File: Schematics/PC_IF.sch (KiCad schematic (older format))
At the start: 4 parts

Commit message: annotate
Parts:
- gave numbers to parts that had none: 4
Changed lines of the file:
@@
 AR Path="/5D2C0CA7/5DD0E967" Ref="U?"  Part="1"
 AR Path="/5D7BE200/5DD0E967" Ref="U?"  Part="1"
-AR Path="/5D8005AF/5D833E4B/5DD0E967" Ref="U?"  Part="1"
-F 0 "U?" H 5250 3350 50  0000 C CNN
+AR Path="/5D8005AF/5D833E4B/5DD0E967" Ref="U24"  Part="1"
+F 0 "U24" H 5250 3350 50  0000 C CNN
 F 1 "74F377" H 5250 3250 50  0000 C CNN
 F 2 "" H 5500 2550 50  0001 C CNN
@@
 AR Path="/5D2C0CA7/5DD0E9D6" Ref="U?"  Part="1"
 AR Path="/5D7BE200/5DD0E9D6" Ref="U?"  Part="1"
-AR Path="/5D8005AF/5D833E4B/5DD0E9D6" Ref="U?"  Part="1"
-F 0 "U?" H 5250 5500 50  0000 C CNN
+AR Path="/5D8005AF/5D833E4B/5DD0E9D6" Ref="U25"  Part="1"
+F 0 "U25" H 5250 5500 50  0000 C CNN
 F 1 "74F377" H 5250 5400 50  0000 C CNN
 F 2 "" H 5500 4700 50  0001 C CNN
@@
 $EndComp
 $Comp
-L power:VCC #PWR?
+L power:VCC #PWR0150
 U 1 1 5DD10B91
 P 5500 1750
-F 0 "#PWR?" H 5500 1600 50  0001 C CNN
+F 0 "#PWR0150" H 5500 1600 50  0001 C CNN
 F 1 "VCC" H 5517 1923 50  0000 C CNN
 F 2 "" H 5500 1750 50  0001 C CNN
@@
 $EndComp
 $Comp
-L power:VCC #PWR?
+L power:VCC #PWR0151
 U 1 1 5DD11404
 P 5500 3900
-F 0 "#PWR?" H 5500 3750 50  0001 C CNN
+F 0 "#PWR0151" H 5500 3750 50  0001 C CNN
 F 1 "VCC" H 5517 4073 50  0000 C CNN
 F 2 "" H 5500 3900 50  0001 C CNN
@@
 $EndComp
 $Comp
-L power:GND #PWR?
+L power:GND #PWR0152
 U 1 1 5DD11B50
 P 5500 3350
-F 0 "#PWR?" H 5500 3100 50  0001 C CNN
+F 0 "#PWR0152" H 5500 3100 50  0001 C CNN
 F 1 "GND" H 5505 3177 50  0000 C CNN
 F 2 "" H 5500 3350 50  0001 C CNN
@@
 $EndComp
 $Comp
-L power:GND #PWR?
+L power:GND #PWR0153
 U 1 1 5DD12126
 P 5500 5500
-F 0 "#PWR?" H 5500 5250 50  0001 C CNN
+F 0 "#PWR0153" H 5500 5250 50  0001 C CNN
 F 1 "GND" H 5505 5327 50  0000 C CNN
 F 2 "" H 5500 5500 50  0001 C CNN
@@
 	5000 5100 3400 5100
 $Comp
-L power:GND #PWR?
+L power:GND #PWR0154
 U 1 1 5DD12CA4
 P 5000 5200
-F 0 "#PWR?" H 5000 4950 50  0001 C CNN
+F 0 "#PWR0154" H 5000 4950 50  0001 C CNN
 F 1 "GND" V 5005 5072 50  0000 R CNN
 F 2 "" H 5000 5200 50  0001 C CNN
@@
 $EndComp
 $Comp
-L power:GND #PWR?
+L power:GND #PWR0155
 U 1 1 5DD131DF
 P 5000 3050
-F 0 "#PWR?" H 5000 2800 50  0001 C CNN
+F 0 "#PWR0155" H 5000 2800 50  0001 C CNN
 F 1 "GND" V 5005 2922 50  0000 R CNN
 F 2 "" H 5000 3050 50  0001 C CNN
@@
 	8850 5500 6600 5500
 $Comp
-L Device:C C?
+L Device:C C21
 U 1 1 5DD31495
 P 1000 7150
-F 0 "C?" H 1115 7196 50  0000 L CNN
+F 0 "C21" H 1115 7196 50  0000 L CNN
 F 1 "100nF" H 1115 7105 50  0000 L CNN
 F 2 "" H 1038 7000 50  0001 C CNN
@@
 $EndComp
 $Comp
-L Device:C C?
+L Device:C C22
 U 1 1 5DD3149B
 P 1500 7150
-F 0 "C?" H 1615 7196 50  0000 L CNN
+F 0 "C22" H 1615 7196 50  0000 L CNN
 F 1 "100nF" H 1615 7105 50  0000 L CNN
 F 2 "" H 1538 7000 50  0001 C CNN
@@
 $EndComp
 $Comp
-L power:GND #PWR?
+L power:GND #PWR0156
 U 1 1 5DD314A1
 P 1000 7300
-F 0 "#PWR?" H 1000 7050 50  0001 C CNN
+F 0 "#PWR0156" H 1000 7050 50  0001 C CNN
 F 1 "GND" H 1005 7127 50  0000 C CNN
 F 2 "" H 1000 7300 50  0001 C CNN
@@
 $EndComp
 $Comp
-L power:VCC #PWR?
+L power:VCC #PWR0157
 U 1 1 5DD314A7
 P 1000 7000
-F 0 "#PWR?" H 1000 6850 50  0001 C CNN
+F 0 "#PWR0157" H 1000 6850 50  0001 C CNN
 F 1 "VCC" H 1017 7173 50  0000 C CNN
 F 2 "" H 1000 7000 50  0001 C CNN

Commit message: Add footprints to all decoupling caps
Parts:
- C21, C22: footprint (none) -> Capacitor_THT:C_Disc_D4.3mm_W1.9mm_P5.00mm
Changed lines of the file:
@@
 F 0 "C21" H 1115 7196 50  0000 L CNN
 F 1 "100nF" H 1115 7105 50  0000 L CNN
-F 2 "" H 1038 7000 50  0001 C CNN
+F 2 "Capacitor_THT:C_Disc_D4.3mm_W1.9mm_P5.00mm" H 1038 7000 50  0001 C CNN
 F 3 "~" H 1000 7150 50  0001 C CNN
 	1    1000 7150
@@
 F 0 "C22" H 1615 7196 50  0000 L CNN
 F 1 "100nF" H 1615 7105 50  0000 L CNN
-F 2 "" H 1538 7000 50  0001 C CNN
+F 2 "Capacitor_THT:C_Disc_D4.3mm_W1.9mm_P5.00mm" H 1538 7000 50  0001 C CNN
 F 3 "~" H 1500 7150 50  0001 C CNN
 	1    1500 7150

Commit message: Assign a bunch more footprints. All are assigned now.
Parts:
- U24, U25: footprint (none) -> Package_DIP:DIP-20_W7.62mm
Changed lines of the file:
@@
 F 0 "U24" H 5250 3350 50  0000 C CNN
 F 1 "74F377" H 5250 3250 50  0000 C CNN
-F 2 "" H 5500 2550 50  0001 C CNN
+F 2 "Package_DIP:DIP-20_W7.62mm" H 5500 2550 50  0001 C CNN
 F 3 "http://www.ti.com/lit/gpn/sn74LS377" H 5500 2550 50  0001 C CNN
 	1    5500 2550
@@
 F 0 "U25" H 5250 5500 50  0000 C CNN
 F 1 "74F377" H 5250 5400 50  0000 C CNN
-F 2 "" H 5500 4700 50  0001 C CNN
+F 2 "Package_DIP:DIP-20_W7.62mm" H 5500 4700 50  0001 C CNN
 F 3 "http://www.ti.com/lit/gpn/sn74LS377" H 5500 4700 50  0001 C CNN
 	1    5500 4700

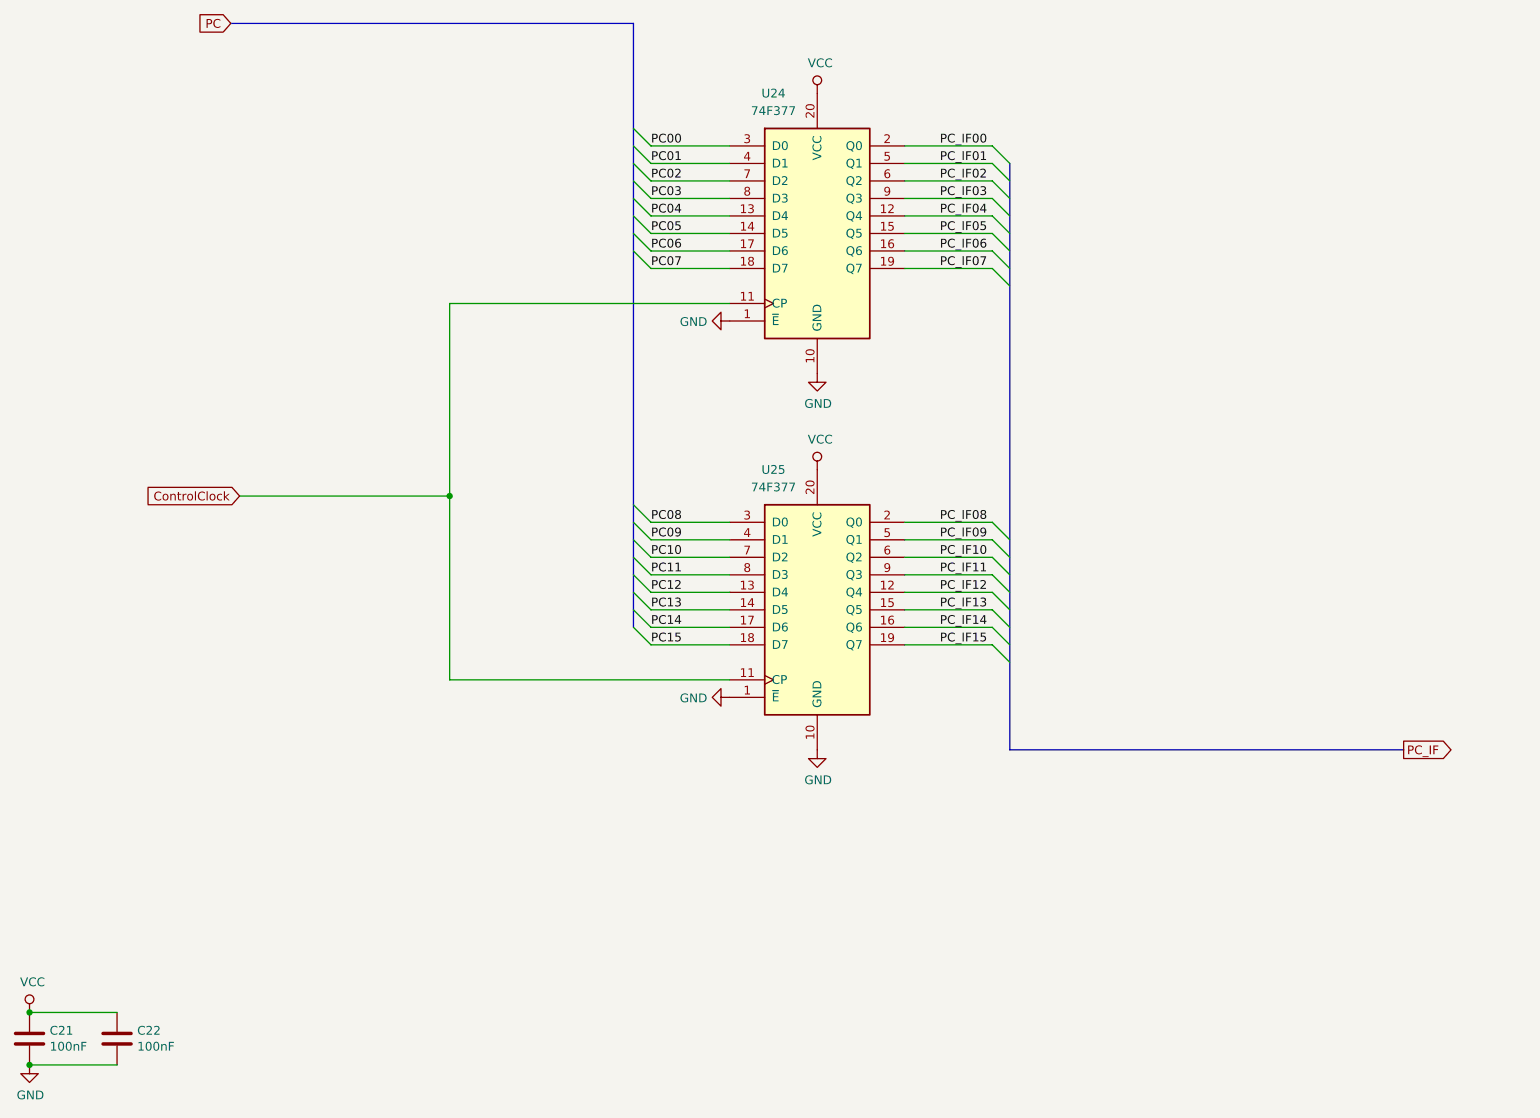
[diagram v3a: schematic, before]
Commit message: My buses were not named according the rules in the Eeschema manual.
Buses which connect to global labels must be named specially.
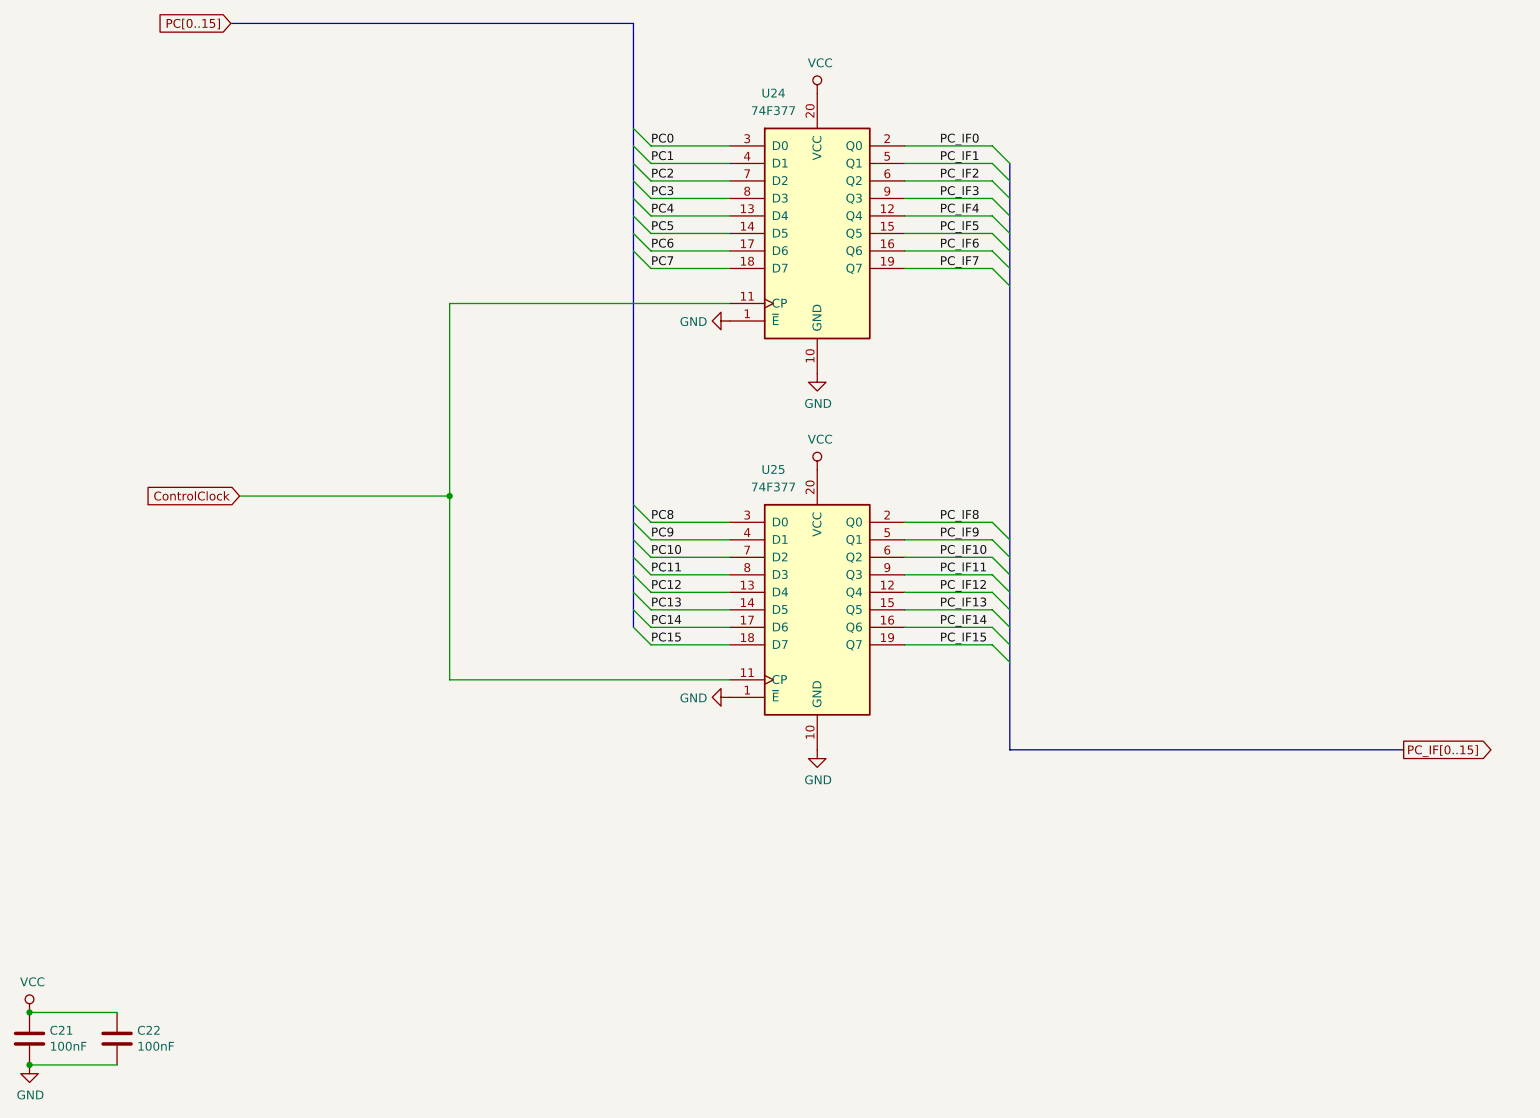
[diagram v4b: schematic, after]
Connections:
- net PC00 renamed PC0
- net PC01 renamed PC1
- net PC02 renamed PC2
- net PC03 renamed PC3
- net PC04 renamed PC4
- net PC05 renamed PC5
- net PC06 renamed PC6
- net PC07 renamed PC7
- net PC08 renamed PC8
- net PC09 renamed PC9
- net PC_IF00 renamed PC_IF0
- net PC_IF01 renamed PC_IF1
- net PC_IF02 renamed PC_IF2
- net PC_IF03 renamed PC_IF3
- net PC_IF04 renamed PC_IF4
- net PC_IF05 renamed PC_IF5
- net PC_IF06 renamed PC_IF6
- net PC_IF07 renamed PC_IF7
- net PC_IF08 renamed PC_IF8
- net PC_IF09 renamed PC_IF9
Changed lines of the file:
@@
 	3400 4050 3400 5100
 Text GLabel 2150 1350 0    50   Input ~ 0
-PC
+PC[0..15]
 Entry Wire Line
 	4550 2050 4450 1950
@@
 	4550 2050 5000 2050
 Text Label 4550 2050 0    50   ~ 0
-PC00
+PC0
 Text Label 4550 2150 0    50   ~ 0
-PC01
+PC1
 Text Label 4550 2250 0    50   ~ 0
-PC02
+PC2
 Text Label 4550 2350 0    50   ~ 0
-PC03
+PC3
 Text Label 4550 2450 0    50   ~ 0
-PC04
+PC4
 Text Label 4550 2550 0    50   ~ 0
-PC05
+PC5
 Text Label 4550 2650 0    50   ~ 0
-PC06
+PC6
 Text Label 4550 2750 0    50   ~ 0
-PC07
+PC7
 Text Label 4550 4200 0    50   ~ 0
-PC08
+PC8
 Text Label 4550 4300 0    50   ~ 0
-PC09
+PC9
 Text Label 4550 4400 0    50   ~ 0
 PC10
@@
 	6500 4900 6000 4900
 Text Label 6200 2050 0    50   ~ 0
-PC_IF00
+PC_IF0
 Text Label 6200 2150 0    50   ~ 0
-PC_IF01
+PC_IF1
 Text Label 6200 2250 0    50   ~ 0
-PC_IF02
+PC_IF2
 Text Label 6200 2350 0    50   ~ 0
-PC_IF03
+PC_IF3
 Text Label 6200 2450 0    50   ~ 0
-PC_IF04
+PC_IF4
 Text Label 6200 2550 0    50   ~ 0
-PC_IF05
+PC_IF5
 Text Label 6200 2650 0    50   ~ 0
-PC_IF06
+PC_IF6
 Text Label 6200 2750 0    50   ~ 0
-PC_IF07
+PC_IF7
 Text Label 6200 4200 0    50   ~ 0
-PC_IF08
+PC_IF8
 Text Label 6200 4300 0    50   ~ 0
-PC_IF09
+PC_IF9
 Text Label 6200 4400 0    50   ~ 0
 PC_IF10
@@
 PC_IF15
 Text GLabel 8850 5500 2    50   Output ~ 0
-PC_IF
+PC_IF[0..15]
 Wire Bus Line
 	8850 5500 6600 5500

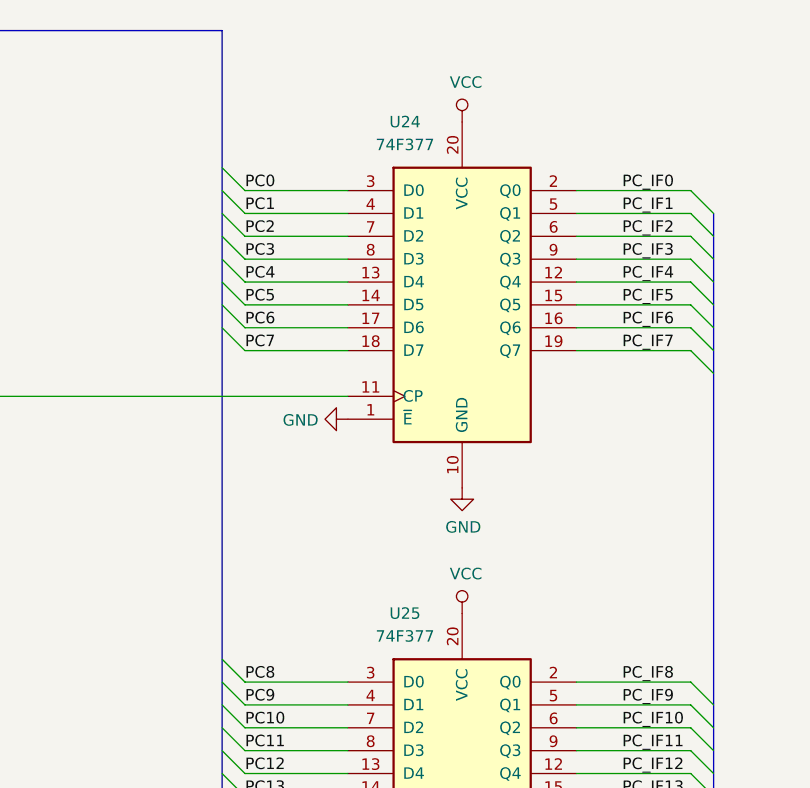
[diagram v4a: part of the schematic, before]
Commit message: Add unused IC units to Output Display to ensure no ICs are shared with other modules.
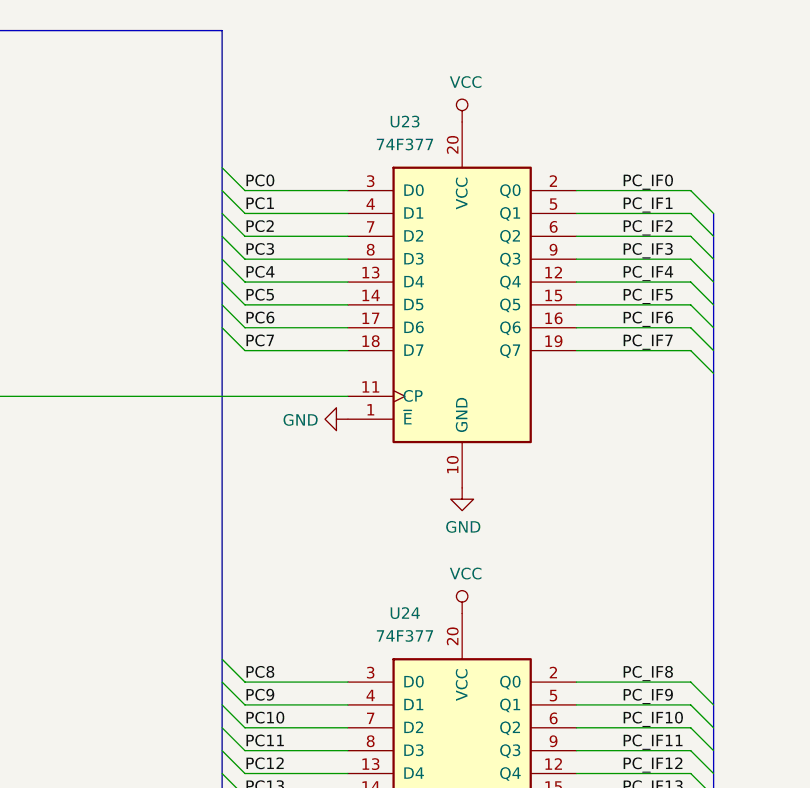
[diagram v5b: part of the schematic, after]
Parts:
- renumbered U24 to U23, U25 to U24
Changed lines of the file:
@@
 AR Path="/5D2C0CA7/5DD0E967" Ref="U?"  Part="1"
 AR Path="/5D7BE200/5DD0E967" Ref="U?"  Part="1"
-AR Path="/5D8005AF/5D833E4B/5DD0E967" Ref="U24"  Part="1"
-F 0 "U24" H 5250 3350 50  0000 C CNN
+AR Path="/5D8005AF/5D833E4B/5DD0E967" Ref="U23"  Part="1"
+F 0 "U23" H 5250 3350 50  0000 C CNN
 F 1 "74F377" H 5250 3250 50  0000 C CNN
 F 2 "Package_DIP:DIP-20_W7.62mm" H 5500 2550 50  0001 C CNN
@@
 AR Path="/5D2C0CA7/5DD0E9D6" Ref="U?"  Part="1"
 AR Path="/5D7BE200/5DD0E9D6" Ref="U?"  Part="1"
-AR Path="/5D8005AF/5D833E4B/5DD0E9D6" Ref="U25"  Part="1"
-F 0 "U25" H 5250 5500 50  0000 C CNN
+AR Path="/5D8005AF/5D833E4B/5DD0E9D6" Ref="U24"  Part="1"
+F 0 "U24" H 5250 5500 50  0000 C CNN
 F 1 "74F377" H 5250 5400 50  0000 C CNN
 F 2 "Package_DIP:DIP-20_W7.62mm" H 5500 4700 50  0001 C CNN
@@
 $EndComp
 $Comp
-L power:VCC #PWR0150
+L power:VCC #PWR054
 U 1 1 5DD10B91
 P 5500 1750
-F 0 "#PWR0150" H 5500 1600 50  0001 C CNN
+F 0 "#PWR054" H 5500 1600 50  0001 C CNN
 F 1 "VCC" H 5517 1923 50  0000 C CNN
 F 2 "" H 5500 1750 50  0001 C CNN
@@
 $EndComp
 $Comp
-L power:VCC #PWR0151
+L power:VCC #PWR056
 U 1 1 5DD11404
 P 5500 3900
-F 0 "#PWR0151" H 5500 3750 50  0001 C CNN
+F 0 "#PWR056" H 5500 3750 50  0001 C CNN
 F 1 "VCC" H 5517 4073 50  0000 C CNN
 F 2 "" H 5500 3900 50  0001 C CNN
@@
 $EndComp
 $Comp
-L power:GND #PWR0152
+L power:GND #PWR055
 U 1 1 5DD11B50
 P 5500 3350
-F 0 "#PWR0152" H 5500 3100 50  0001 C CNN
+F 0 "#PWR055" H 5500 3100 50  0001 C CNN
 F 1 "GND" H 5505 3177 50  0000 C CNN
 F 2 "" H 5500 3350 50  0001 C CNN
@@
 $EndComp
 $Comp
-L power:GND #PWR0153
+L power:GND #PWR057
 U 1 1 5DD12126
 P 5500 5500
-F 0 "#PWR0153" H 5500 5250 50  0001 C CNN
+F 0 "#PWR057" H 5500 5250 50  0001 C CNN
 F 1 "GND" H 5505 5327 50  0000 C CNN
 F 2 "" H 5500 5500 50  0001 C CNN
@@
 	5000 5100 3400 5100
 $Comp
-L power:GND #PWR0154
+L power:GND #PWR053
 U 1 1 5DD12CA4
 P 5000 5200
-F 0 "#PWR0154" H 5000 4950 50  0001 C CNN
+F 0 "#PWR053" H 5000 4950 50  0001 C CNN
 F 1 "GND" V 5005 5072 50  0000 R CNN
 F 2 "" H 5000 5200 50  0001 C CNN
@@
 $EndComp
 $Comp
-L power:GND #PWR0155
+L power:GND #PWR052
 U 1 1 5DD131DF
 P 5000 3050
-F 0 "#PWR0155" H 5000 2800 50  0001 C CNN
+F 0 "#PWR052" H 5000 2800 50  0001 C CNN
 F 1 "GND" V 5005 2922 50  0000 R CNN
 F 2 "" H 5000 3050 50  0001 C CNN
@@
 $EndComp
 $Comp
-L power:GND #PWR0156
+L power:GND #PWR051
 U 1 1 5DD314A1
 P 1000 7300
-F 0 "#PWR0156" H 1000 7050 50  0001 C CNN
+F 0 "#PWR051" H 1000 7050 50  0001 C CNN
 F 1 "GND" H 1005 7127 50  0000 C CNN
 F 2 "" H 1000 7300 50  0001 C CNN
@@
 $EndComp
 $Comp
-L power:VCC #PWR0157
+L power:VCC #PWR050
 U 1 1 5DD314A7
 P 1000 7000
-F 0 "#PWR0157" H 1000 6850 50  0001 C CNN
+F 0 "#PWR050" H 1000 6850 50  0001 C CNN
 F 1 "VCC" H 1017 7173 50  0000 C CNN
 F 2 "" H 1000 7000 50  0001 C CNN

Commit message: Add unused IC units to Data RAM to ensure no ICs are shared with other modules.
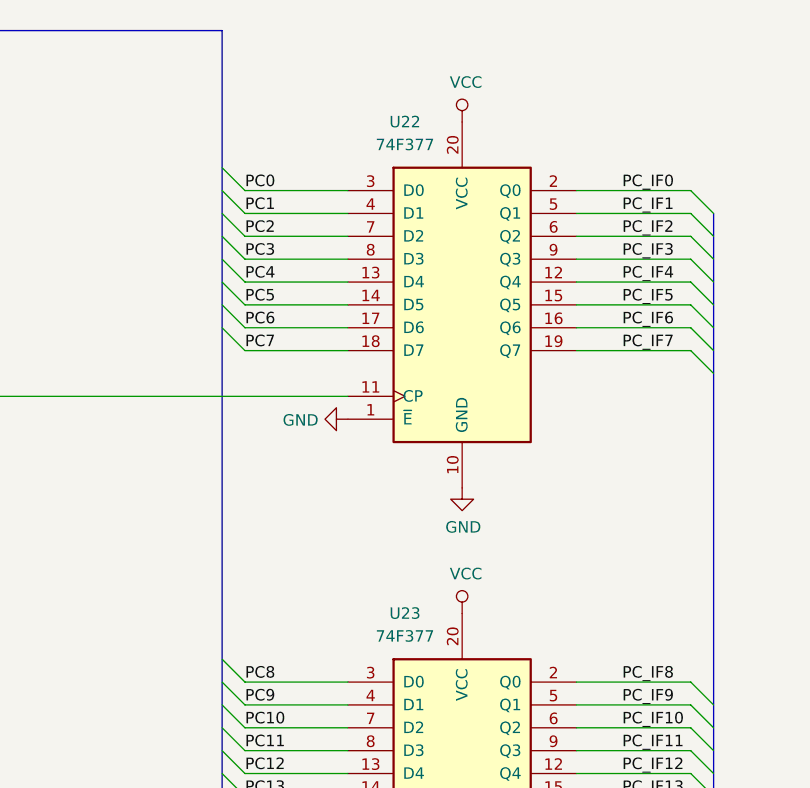
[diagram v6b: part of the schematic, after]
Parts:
- renumbered U23 to U22, U24 to U23
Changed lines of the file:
@@
 AR Path="/5D2C0CA7/5DD0E967" Ref="U?"  Part="1"
 AR Path="/5D7BE200/5DD0E967" Ref="U?"  Part="1"
-AR Path="/5D8005AF/5D833E4B/5DD0E967" Ref="U23"  Part="1"
-F 0 "U23" H 5250 3350 50  0000 C CNN
+AR Path="/5D8005AF/5D833E4B/5DD0E967" Ref="U22"  Part="1"
+F 0 "U22" H 5250 3350 50  0000 C CNN
 F 1 "74F377" H 5250 3250 50  0000 C CNN
 F 2 "Package_DIP:DIP-20_W7.62mm" H 5500 2550 50  0001 C CNN
@@
 AR Path="/5D2C0CA7/5DD0E9D6" Ref="U?"  Part="1"
 AR Path="/5D7BE200/5DD0E9D6" Ref="U?"  Part="1"
-AR Path="/5D8005AF/5D833E4B/5DD0E9D6" Ref="U24"  Part="1"
-F 0 "U24" H 5250 5500 50  0000 C CNN
+AR Path="/5D8005AF/5D833E4B/5DD0E9D6" Ref="U23"  Part="1"
+F 0 "U23" H 5250 5500 50  0000 C CNN
 F 1 "74F377" H 5250 5400 50  0000 C CNN
 F 2 "Package_DIP:DIP-20_W7.62mm" H 5500 4700 50  0001 C CNN
